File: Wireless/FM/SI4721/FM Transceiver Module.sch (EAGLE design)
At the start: 29 parts, among them CN1 35RASMT4BHNTRX, U1 SI4721, Y1 CRYSTAL.ABS07

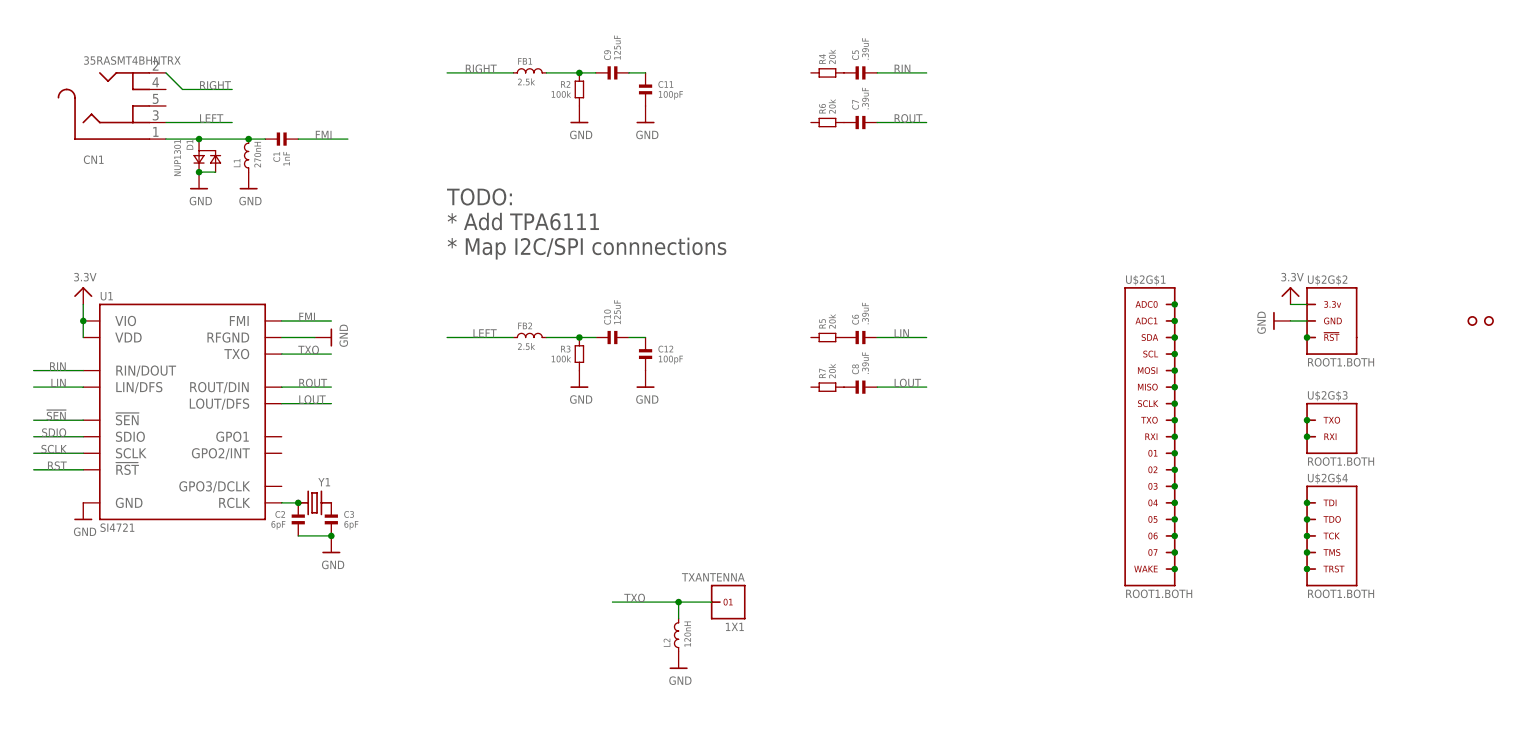
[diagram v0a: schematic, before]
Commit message: Completed schematic for FM Transceiver (SI4721) Layout completed. Routing needed...
Signed-off-by: Cruz Monrreal II <Cruz.Monrreal@gmail.com>
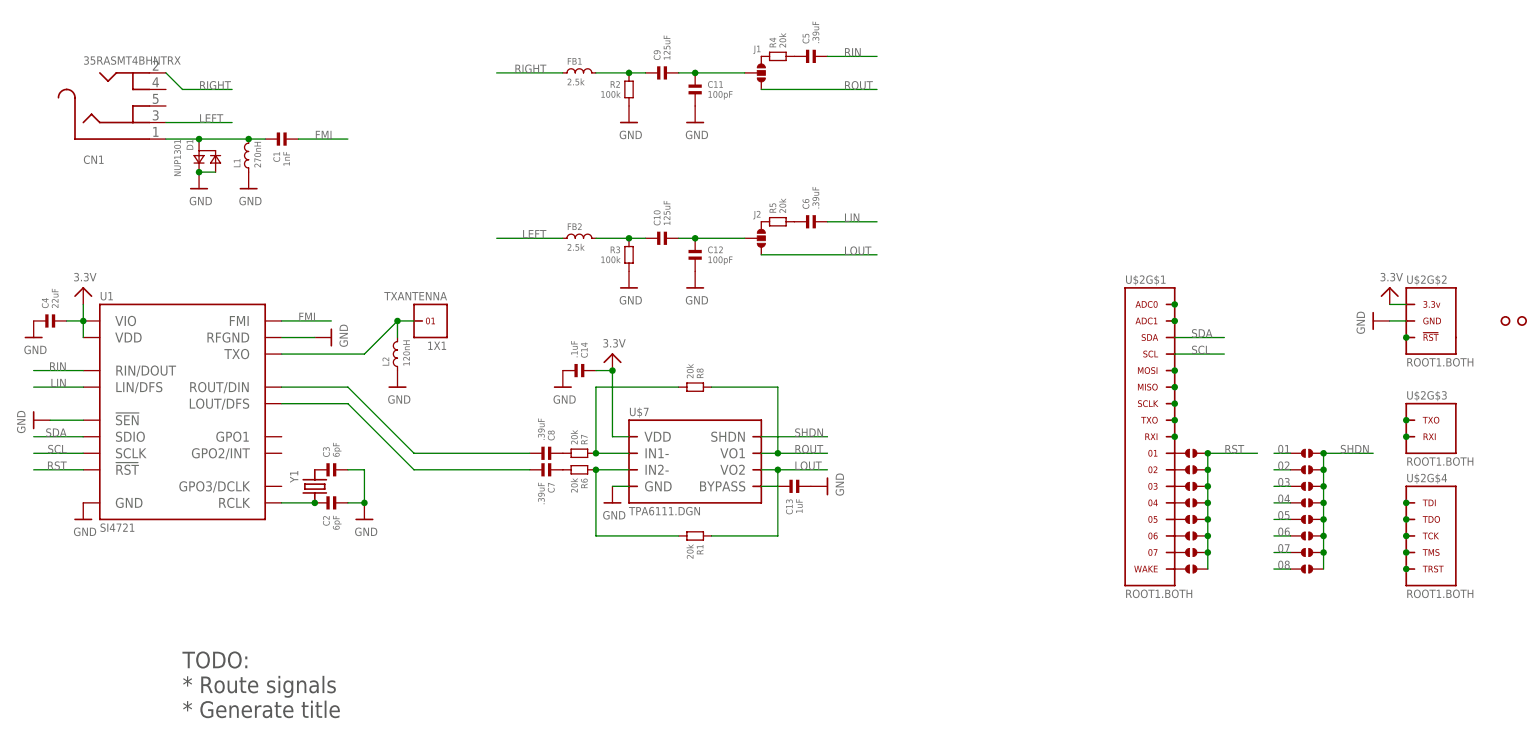
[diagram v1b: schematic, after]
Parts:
- added C13: 1uF, .standardparts:CAPACITOR.0603
- added C14: .1uF, .standardparts:CAPACITOR.0603
- added C4: 22uF, .standardparts:CAPACITOR.0805
- added J1, J2: (no value), .solderjumper:SOLDERJUMPER.3.LRG.12
- added J10, J11, J12, J13, J14, J15, J16, J17, J18, J3, J4, J5, J6, J7, J8, J9: (no value), .solderjumper:SOLDERJUMPER.2.SML
- added R1, R8: 20k, .standardparts:RESISTOR.0603
- added U$7: TPA6111.DGN, .packages(ti):TPA6111.DGN
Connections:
- removed net !SEN!: U1.!SEN
- removed net N$1: U$2G$1.04
- removed net N$10: U$2G$1.01
- removed net N$11: U$2G$1.02
- removed net N$14: U$2G$1.05
- removed net N$15: U$2G$1.06
- removed net N$16: U$2G$1.07
- removed net N$17: U$2G$1.WAKE
- removed net N$4: U$2G$1.SCL
- removed net N$5: U$2G$1.03
- removed net SCLK: U1.SCLK
- removed net SDIO: U1.SDIO
- new net 01: J11.1, J3.1, U$2G$1.01
- new net 02: J12.1, J4.1, U$2G$1.02
- new net 03: J13.1, J5.1, U$2G$1.03
- new net 04: J14.1, J6.1, U$2G$1.04
- new net 05: J15.1, J7.1, U$2G$1.05
- new net 06: J16.1, J8.1, U$2G$1.06
- new net 07: J17.1, J9.1, U$2G$1.07
- new net 08: J10.1, J18.1, U$2G$1.WAKE
- new net LOUT.AMP: C7.2, U1.LOUT/DFS
- new net N$26: R7.1, R8.2, U$7.IN1-
- new net N$39: R1.2, R6.1, U$7.IN2-
- new net N$42: J2.1, R5.1
- new net N$43: J1.1, R4.1
- new net ROUT.AMP: C8.2, U1.ROUT/DIN
- new net SCL: U$2G$1.SCL, U1.SCLK
- new net SDA: U$2G$1.SDA, U1.SDIO
- new net SHDN: J11.2, J12.2, J13.2, J14.2, J15.2, J16.2, J17.2, J18.2, U$7.SHDN
- net 3.3V: now also C14.1, C4.2, U$7.VDD
- net GND: now also C13.2, C14.2, C4.1, U$7.GND, U1.!SEN
- net LOUT: now also J2.3, R1.1, U$7.VO2; no longer C8.2, U1.LOUT/DFS
- net N$29: now also J1.2
- net N$3: now also C13.1, U$7.BYPASS; no longer U$2G$1.SDA
- net N$32: now also J2.2
- net ROUT: now also J1.3, R8.1, U$7.VO1; no longer C7.2, U1.ROUT/DIN
- net RST: now also J10.2, J3.2, J4.2, J5.2, J6.2, J7.2, J8.2, J9.2
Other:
- note added: "TODO: * Route signals * Generate title"
- note removed: "TODO: * Add TPA6111 * Map I2C/SPI connnections"
- moved on the sheet: C10, C11, C12, C2, C3, C5, C6, C7, C8, C9, FB1, FB2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

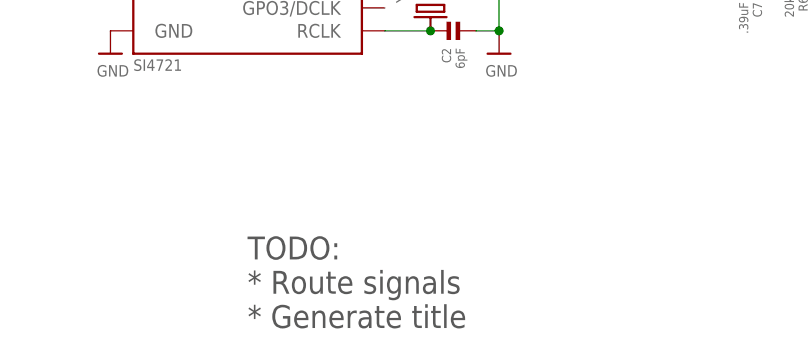
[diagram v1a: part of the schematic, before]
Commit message: Completed FM Transceiver Module
Signed-off-by: Cruz Monrreal II <Cruz.Monrreal@gmail.com>
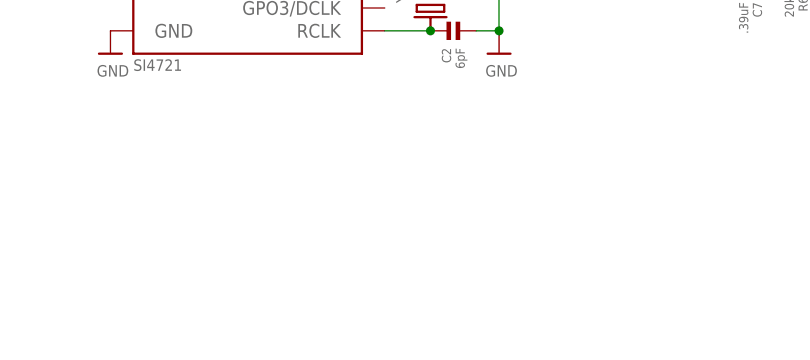
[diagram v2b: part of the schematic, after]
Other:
- note removed: "TODO: * Route signals * Generate title"
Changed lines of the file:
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@@
 <sheet>
 <plain>
-<text x="33.02" y="66.04" size="2.54" layer="97">TODO:
-* Route signals
-* Generate title</text>
 </plain>
 <instances>
@@
 </schematic>
 </drawing>
-<compatibility>
-<note version="6.3" minversion="6.2.2" severity="warning">
-Since Version 6.2.2 text objects can contain more than one line,
-which will not be processed correctly with this version.
-</note>
-</compatibility>
 </eagle>
